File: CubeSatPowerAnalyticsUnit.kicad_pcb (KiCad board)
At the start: 2 copper layers, 30 x 30 mm, 17 parts, among them J1 Conn_01x05_Pin, Q1 2N7002, T1 V_In (3,3V), T2 V_Out, T3 GND, T4 UART

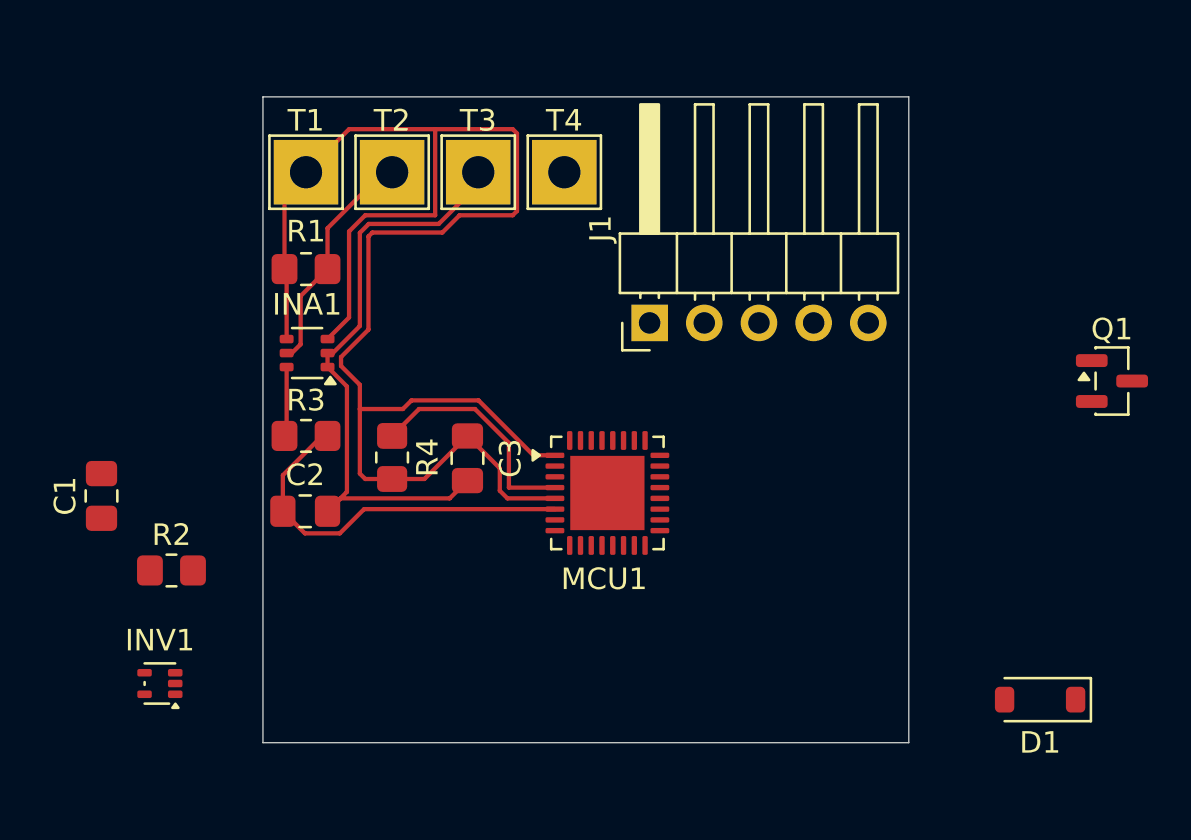
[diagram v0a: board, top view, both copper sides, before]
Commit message: Start PCB layout and initial routing.
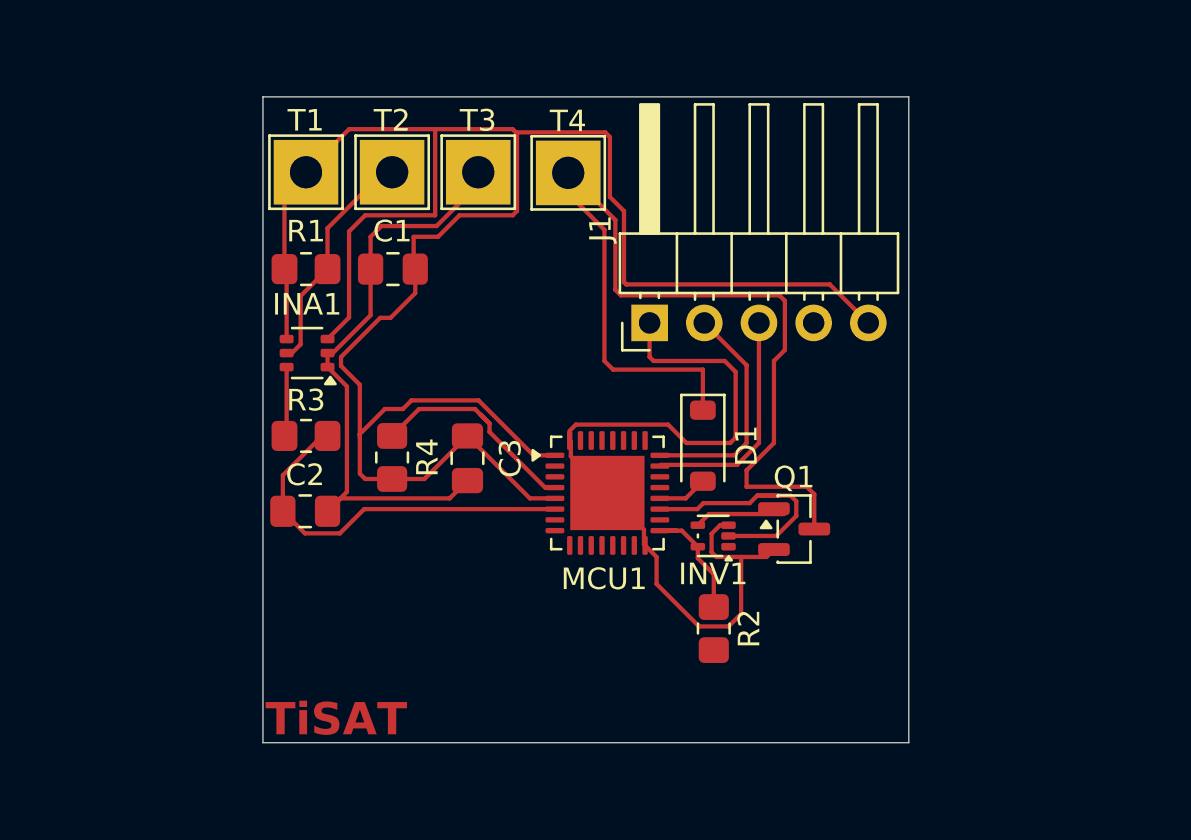
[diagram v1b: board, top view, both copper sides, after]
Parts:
- moved INV1 26.6 mm to (170.9, 120.4)
- moved R2 25.3 mm to (170.9, 124.7), turned to -90 degrees
- moved D1 19.6 mm to (170.4, 116.2), turned to -90 degrees
- moved C1 17.2 mm to (156.0, 108.0), turned to 180 degrees
- moved Q1 16.3 mm to (174.7, 120.1)
- moved T4 0.18 mm to (164.2, 103.5)
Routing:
- net Net-(D1-K): track 0.00 -> 44.8 mm
- net GND: track 28.5 -> 66.7 mm
- net VREF (3,3V): track 77.7 -> 106.4 mm
- net Net-(MCU1-PA9): track 0.00 -> 12.0 mm
- net /SWCLK: track 0.00 -> 10.7 mm
- net /SWDIO: track 0.00 -> 10.6 mm
- net Net-(Q1-G): track 0.00 -> 4.23 mm
- net Net-(D1-A): track 0.00 -> 2.33 mm
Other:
- board text added: "TiSAT"

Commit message: Initial commit - KiCad project v1.2
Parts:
- removed INV1: 74LVC1GU04DRL, Package_TO_SOT_SMD:SOT-553
- removed R4: 10K Ohm, Resistor_SMD:R_0805_2012Metric_Pad1.20x1.40mm_HandSolder
- R2: value 4K7 Ohm -> 1K Ohm
- R3: value 1K Ohm -> 10K Ohm
- moved R2 18.9 mm to (156.5, 112.5), turned to 0 degrees
- moved R3 10.9 mm to (160.5, 109.0), turned to 180 degrees
- moved INA1 5.67 mm to (156.6, 108.5)
- moved C2 5.55 mm to (156.5, 116.0), turned to 180 degrees
- moved C1 5.00 mm to (152.5, 111.5), turned to 0 degrees
- moved C3 4.38 mm to (160.5, 112.5), turned to 180 degrees
- moved D1 2.34 mm to (172.6, 117.1), turned to 180 degrees
- moved Q1 2.03 mm to (172.6, 120.2)
- moved R1 0.50 mm to (152.5, 108.0)
- moved T4 0.18 mm to (164.0, 103.5)
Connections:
- Q1 pad 1: Net-(Q1-G) -> Net-(MCU1-PA9)
- R2 pad 1: VREF (3,3V) -> Net-(INA1-Pad6)
- R2 pad 2: Net-(D1-K) -> /ADC1_IN5
- R3 pad 1: Net-(INA1-Pad6) -> /RST
- R3 pad 2: /ADC1_IN5 -> VREF (3,3V)
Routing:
- net VREF (3,3V): track 106.4 -> 62.3 mm, vias 0 -> 6
- net GND: track 66.7 -> 27.0 mm, vias 0 -> 4
- net /RST: track 10.5 -> 32.5 mm, vias 0 -> 3
- net Net-(D1-K): track 44.8 -> 30.4 mm, vias 0 -> 2
- net Net-(MCU1-PA9): track 12.0 -> 3.29 mm
- net /ADC1_IN5: track 18.0 -> 12.0 mm
- net Net-(Q1-G): track 4.23 -> 0.00 mm
- net /SWCLK: track 10.7 -> 7.54 mm
- net Net-(INA1--): track 10.8 -> 7.82 mm
- net /SWDIO: track 10.6 -> 9.20 mm
- net Net-(D1-A): track 2.33 -> 3.44 mm
- added copper zone on B.Cu, net GND

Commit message: Update PCB design - KiCad project v1.3
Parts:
- R1: value 0,1 Ohm -> 50 mOhm
- T1, T2, T3, T4: footprint TestPoint:TestPoint_THTPad_3.0x3.0mm_Drill1.5mm -> TestPoint:TestPoint_Pad_3.0x3.0mm
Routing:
- net VREF (3,3V): track 62.3 -> 76.2 mm
- net GND: track 27.0 -> 35.7 mm, vias 4 -> 5

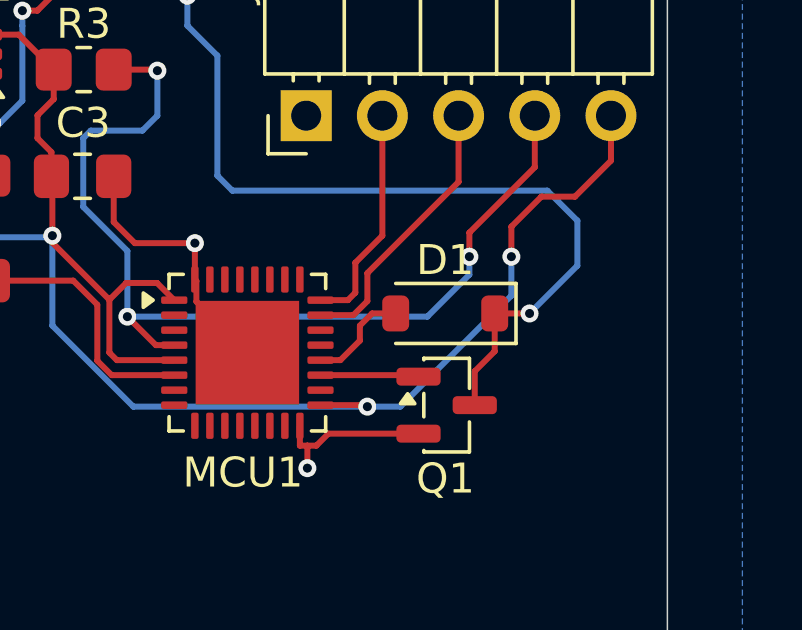
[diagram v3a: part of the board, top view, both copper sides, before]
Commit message: Modify various footprints - KiCad project v1.5
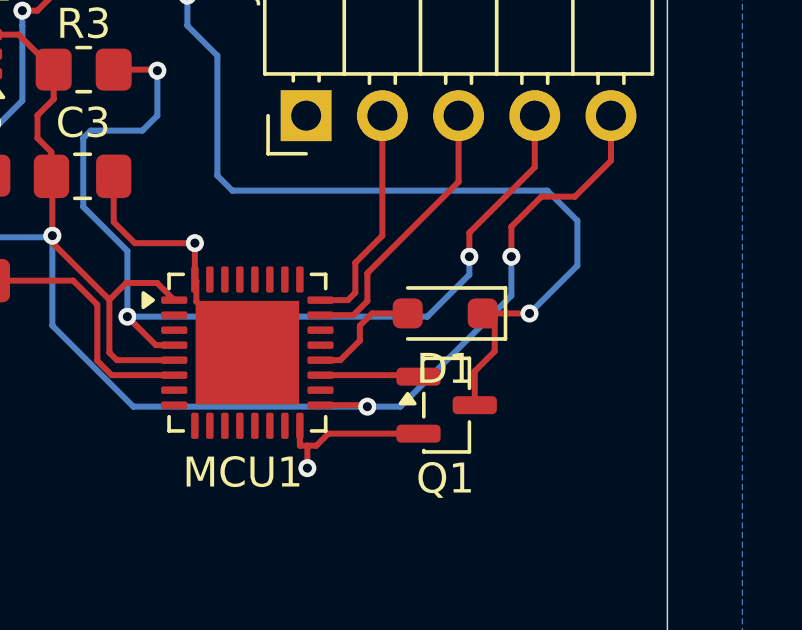
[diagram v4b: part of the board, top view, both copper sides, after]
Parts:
- D1: footprint Diode_SMD:D_SOD-123 -> Diode_SMD:D_SOD-323_HandSoldering
- R1: value 50 mOhm -> 0.05 Ohm
